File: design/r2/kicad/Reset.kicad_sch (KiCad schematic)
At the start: 12 parts, among them IC15 555N

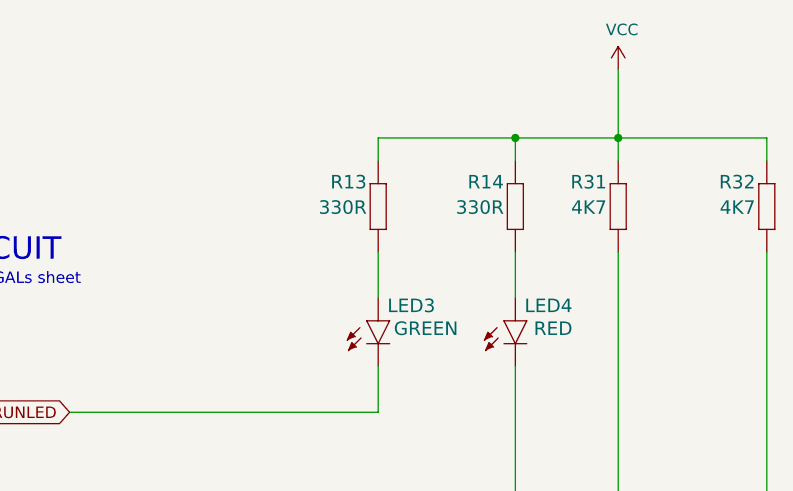
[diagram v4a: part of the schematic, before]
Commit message: Tentative r2 SMD design
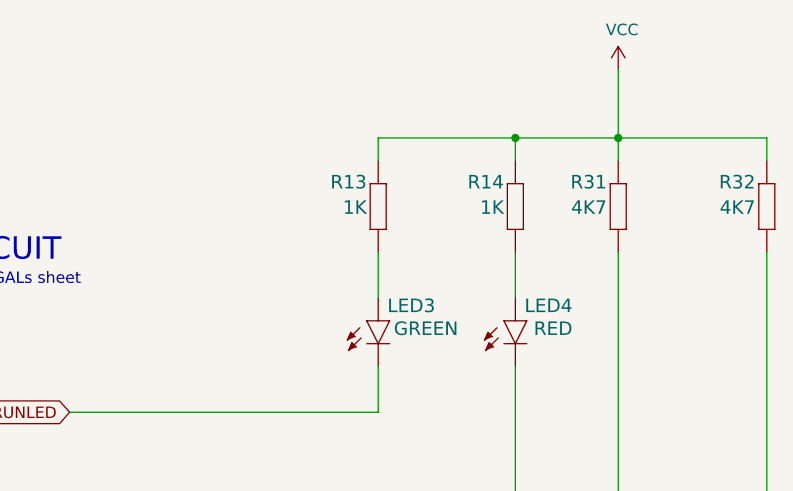
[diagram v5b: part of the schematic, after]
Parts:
- C13: footprint rosco_m68k:C2.5-3 -> Capacitor_SMD:C_0603_1608Metric
- R13, R14: value 330R -> 1K; footprint rosco_m68k:0207_10 -> Resistor_SMD:R_0603_1608Metric
- R27, R28, R31, R32: footprint rosco_m68k:0207_10 -> Resistor_SMD:R_0603_1608Metric
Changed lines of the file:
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@@
       (effects (font (size 1.4986 1.4986)) (justify left bottom))
     )
-    (property "Footprint" "rosco_m68k:0207_10" (at 52.07 68.58 0)
+    (property "Footprint" "Resistor_SMD:R_0603_1608Metric" (at 52.07 68.58 0)
       (effects (font (size 1.27 1.27)) hide)
     )
@@
       (effects (font (size 1.4986 1.4986)) (justify left bottom))
     )
-    (property "Footprint" "rosco_m68k:0207_10" (at 95.25 132.08 0)
+    (property "Footprint" "Resistor_SMD:R_0603_1608Metric" (at 95.25 132.08 0)
       (effects (font (size 1.27 1.27)) hide)
     )
@@
       (effects (font (size 1.4986 1.4986)) (justify left bottom))
     )
-    (property "Value" "330R" (at 203.2 70.358 90)
+    (property "Value" "1K" (at 203.2 70.358 90)
       (effects (font (size 1.4986 1.4986)) (justify left bottom))
     )
-    (property "Footprint" "rosco_m68k:0207_10" (at 204.47 71.12 0)
+    (property "Footprint" "Resistor_SMD:R_0603_1608Metric" (at 204.47 71.12 0)
       (effects (font (size 1.27 1.27)) hide)
     )
@@
       (effects (font (size 1.4986 1.4986)) (justify left bottom))
     )
-    (property "Footprint" "rosco_m68k:0207_10" (at 215.9 71.12 0)
+    (property "Footprint" "Resistor_SMD:R_0603_1608Metric" (at 215.9 71.12 0)
       (effects (font (size 1.27 1.27)) hide)
     )
@@
       (effects (font (size 1.4986 1.4986)) (justify left bottom))
     )
-    (property "Footprint" "rosco_m68k:0207_10" (at 232.41 71.12 0)
+    (property "Footprint" "Resistor_SMD:R_0603_1608Metric" (at 232.41 71.12 0)
       (effects (font (size 1.27 1.27)) hide)
     )
@@
       (effects (font (size 1.4986 1.4986)) (justify left bottom))
     )
-    (property "Value" "330R" (at 187.96 70.358 90)
+    (property "Value" "1K" (at 187.96 70.358 90)
       (effects (font (size 1.4986 1.4986)) (justify left bottom))
     )
-    (property "Footprint" "rosco_m68k:0207_10" (at 189.23 71.12 0)
+    (property "Footprint" "Resistor_SMD:R_0603_1608Metric" (at 189.23 71.12 0)
       (effects (font (size 1.27 1.27)) hide)
     )
@@
       (effects (font (size 1.4986 1.4986)) (justify left bottom))
     )
-    (property "Footprint" "rosco_m68k:C2.5-3" (at 62.23 68.58 0)
+    (property "Footprint" "Capacitor_SMD:C_0603_1608Metric" (at 62.23 68.58 0)
       (effects (font (size 1.27 1.27)) hide)
     )
